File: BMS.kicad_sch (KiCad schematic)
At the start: 63 parts, among them J1 Screw_Terminal_01x02, J5 BATT_PACK -, J6 BATT_PACK -, Q22 CSD19531Q5A, Q23 CSD19531Q5A, Q24 CSD19531Q5A, T3 EE20_10_6_750811647, U1 TL431DBZ, U18 VIPer26LD, U2 PC817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

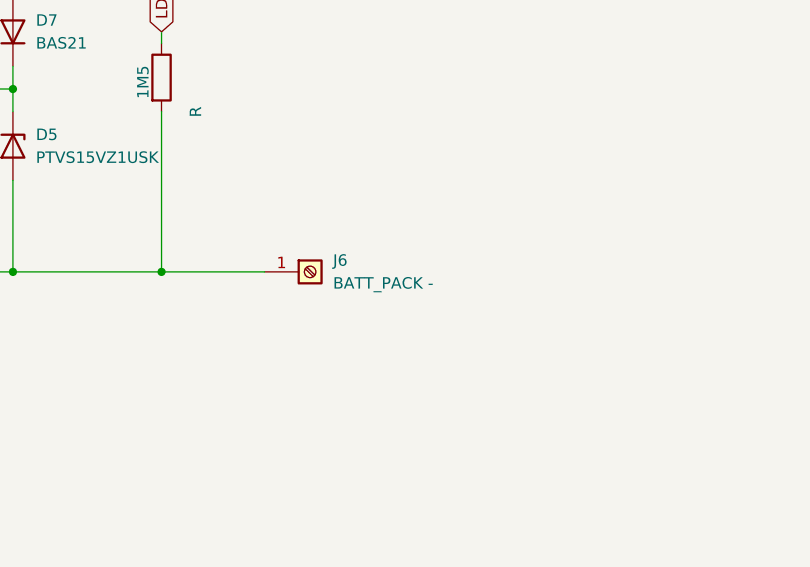
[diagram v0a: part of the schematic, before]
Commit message: Add full KiCad PCB file and backups
Replace the placeholder BMS.kicad_pcb with the complete KiCad PCB data (version 20260206) including layers, setup, footprints, pads and 3D models. Update related project files (BMS.kicad_prl, BMS.kicad_pro, BMS.kicad_sch) and their lock files. Add five new backup archives in BMS-backups (2026-06-19 and multiple 2026-06-20 timestamps).
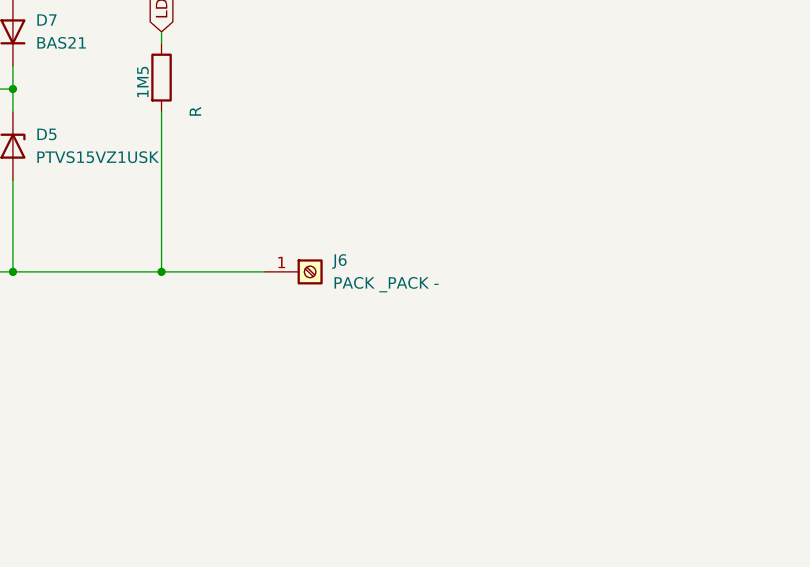
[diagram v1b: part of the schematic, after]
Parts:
- C19, C20, C24, C30, C31, C33, C34, C35, C36, C37, C38: footprint Capacitor_THT:CP_Radial_D5.0mm_P2.00mm -> Capacitor_SMD:C_0402_1005Metric
- J6: value BATT_PACK - -> PACK _PACK -
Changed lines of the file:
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@@
 			)
 		)
-		(property "Value" "BATT_PACK -"
+		(property "Value" "PACK _PACK -"
 			(at 280.67 179.0699 0)
 			(show_name no)
@@
 			)
 		)
-		(property "Footprint" "Capacitor_THT:CP_Radial_D5.0mm_P2.00mm"
+		(property "Footprint" "Capacitor_SMD:C_0402_1005Metric"
 			(at 204.47 204.1652 0)
 			(hide yes)
@@
 			)
 		)
-		(property "Footprint" "Capacitor_THT:CP_Radial_D5.0mm_P2.00mm"
+		(property "Footprint" "Capacitor_SMD:C_0402_1005Metric"
 			(at 127.9652 83.82 0)
 			(hide yes)
@@
 			)
 		)
-		(property "Footprint" "Capacitor_THT:CP_Radial_D5.0mm_P2.00mm"
+		(property "Footprint" "Capacitor_SMD:C_0402_1005Metric"
 			(at 84.1248 219.71 0)
 			(hide yes)
@@
 			)
 		)
-		(property "Footprint" "Capacitor_THT:CP_Radial_D5.0mm_P2.00mm"
+		(property "Footprint" "Capacitor_SMD:C_0402_1005Metric"
 			(at 66.3448 177.8 0)
 			(hide yes)
@@
 			)
 		)
-		(property "Footprint" "Capacitor_THT:CP_Radial_D5.0mm_P2.00mm"
+		(property "Footprint" "Capacitor_SMD:C_0402_1005Metric"
 			(at 222.25 204.1652 0)
 			(hide yes)
@@
 			)
 		)
-		(property "Footprint" "Capacitor_THT:CP_Radial_D5.0mm_P2.00mm"
+		(property "Footprint" "Capacitor_SMD:C_0402_1005Metric"
 			(at 58.42 157.7848 0)
 			(hide yes)
@@
 			)
 		)
-		(property "Footprint" "Capacitor_THT:CP_Radial_D5.0mm_P2.00mm"
+		(property "Footprint" "Capacitor_SMD:C_0402_1005Metric"
 			(at 72.6948 194.31 0)
 			(hide yes)
@@
 			)
 		)
-		(property "Footprint" "Capacitor_THT:CP_Radial_D5.0mm_P2.00mm"
+		(property "Footprint" "Capacitor_SMD:C_0402_1005Metric"
 			(at 182.88 29.5148 0)
 			(hide yes)
@@
 			)
 		)
-		(property "Footprint" "Capacitor_THT:CP_Radial_D5.0mm_P2.00mm"
+		(property "Footprint" "Capacitor_SMD:C_0402_1005Metric"
 			(at 130.5052 46.99 0)
 			(hide yes)
@@
 			)
 		)
-		(property "Footprint" "Capacitor_THT:CP_Radial_D5.0mm_P2.00mm"
+		(property "Footprint" "Capacitor_SMD:C_0402_1005Metric"
 			(at 79.0448 207.01 0)
 			(hide yes)
@@
 			)
 		)
-		(property "Footprint" "Capacitor_THT:CP_Radial_D5.0mm_P2.00mm"
+		(property "Footprint" "Capacitor_SMD:C_0402_1005Metric"
 			(at 44.7548 146.05 0)
 			(hide yes)

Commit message: Battery level indicator LM3914
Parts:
- added C3: 470uF, Capacitor_SMD:C_0805_2012Metric, symbol Device:C_Polarized
- added D10, D11, D12, D13, D14, D15, D16, D6, D8, D9: LED, symbol Device:LED
- added U3: LM3914N, Package_DIP:DIP-18_W7.62mm, symbol Driver_LED:LM3914N
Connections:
- net GND: now also U3.2 (V-)
- net V+: now reaches 2W,5.1Ohm22.2, BT18.1 (+)
- net V+: now also U3.3 (V+)
- new net: D9.1 (K), U3.17 (LED3)
- new net: C3.1, D10.2 (A), D11.2 (A), D12.2 (A), D13.2 (A), D14.2 (A), D15.2 (A), D16.2 (A), D6.2 (A), D8.2 (A), D9.2 (A)
- new net: D13.1 (K), U3.13 (LED7)
- new net: D15.1 (K), U3.11 (LED9)
- new net: D16.1 (K), U3.10 (LED10)
- new net: C3.2, U3.4 (RLO)
- new net: D12.1 (K), U3.14 (LED6)
- new net: D11.1 (K), U3.15 (LED5)
- new net: D10.1 (K), U3.16 (LED4)
- new net: D8.1 (K), U3.18 (LED2)
- new net: D6.1 (K), U3.1 (LED1)
- new net: D14.1 (K), U3.12 (LED8)

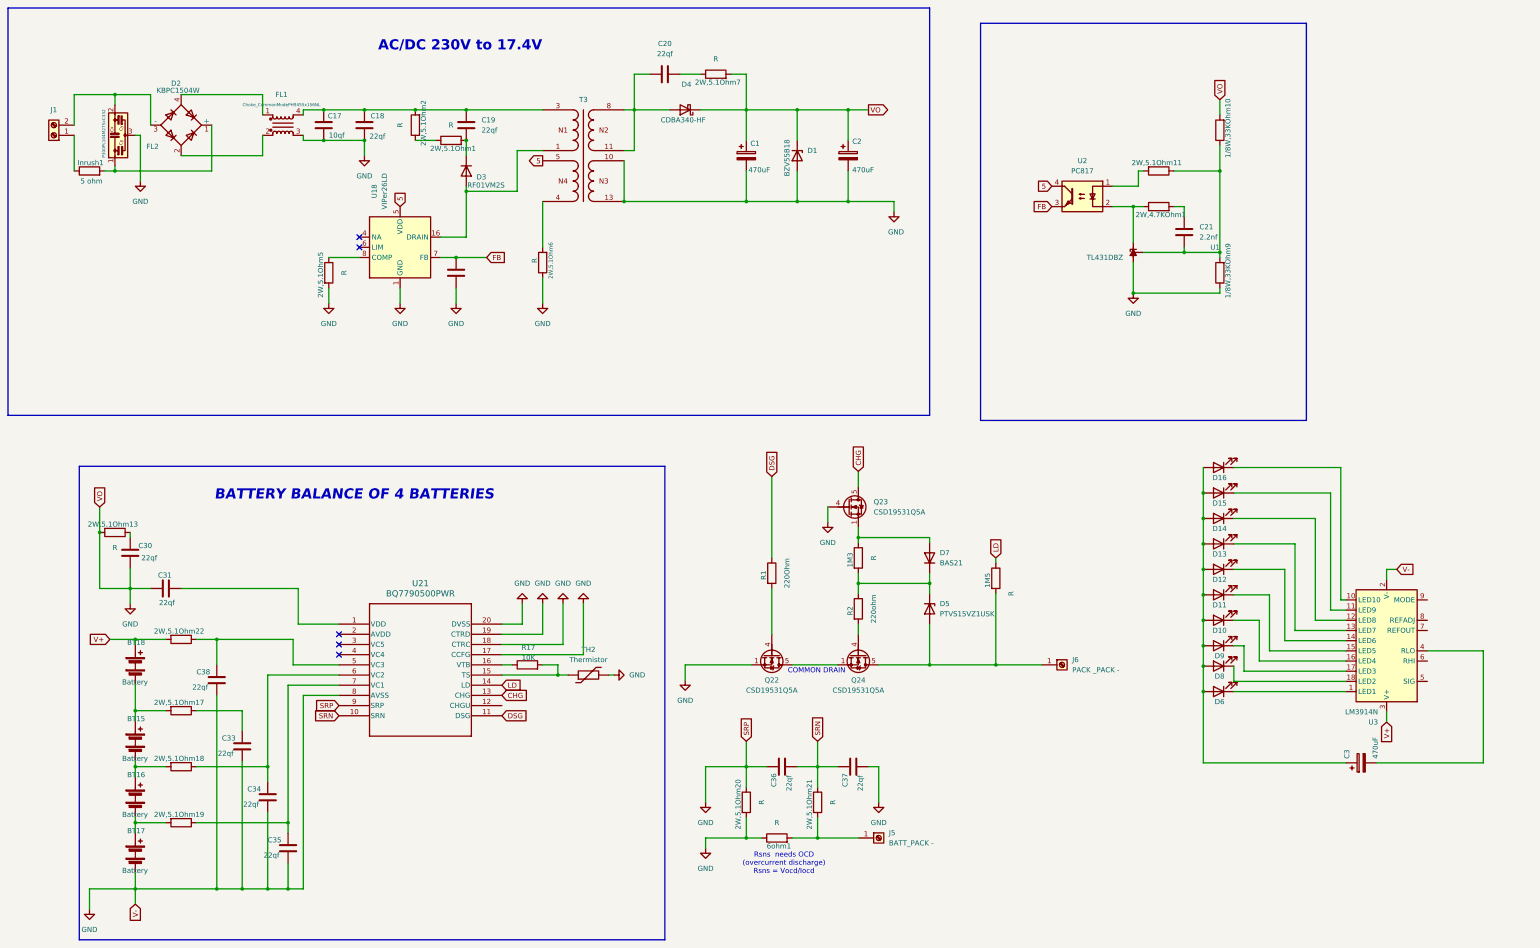
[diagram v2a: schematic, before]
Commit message: Update PCB stackup, footprints, and add backups
Add multiple BMS backup archives and project PNG; modify BMS.kicad_pcb with an explicit stackup (layers, thicknesses, dielectric), enable zone_defaults, and update many footprints and component definitions. Changes include footprint replacements and edits (resistor/pad sizes, SMD 0402→0805 adjustments, pad positions/nets, UUIDs), added/adjusted 3D model references and part rotations/offsets, and new LED/resistor SMD footprints. Also update related KiCad project files and lock files.
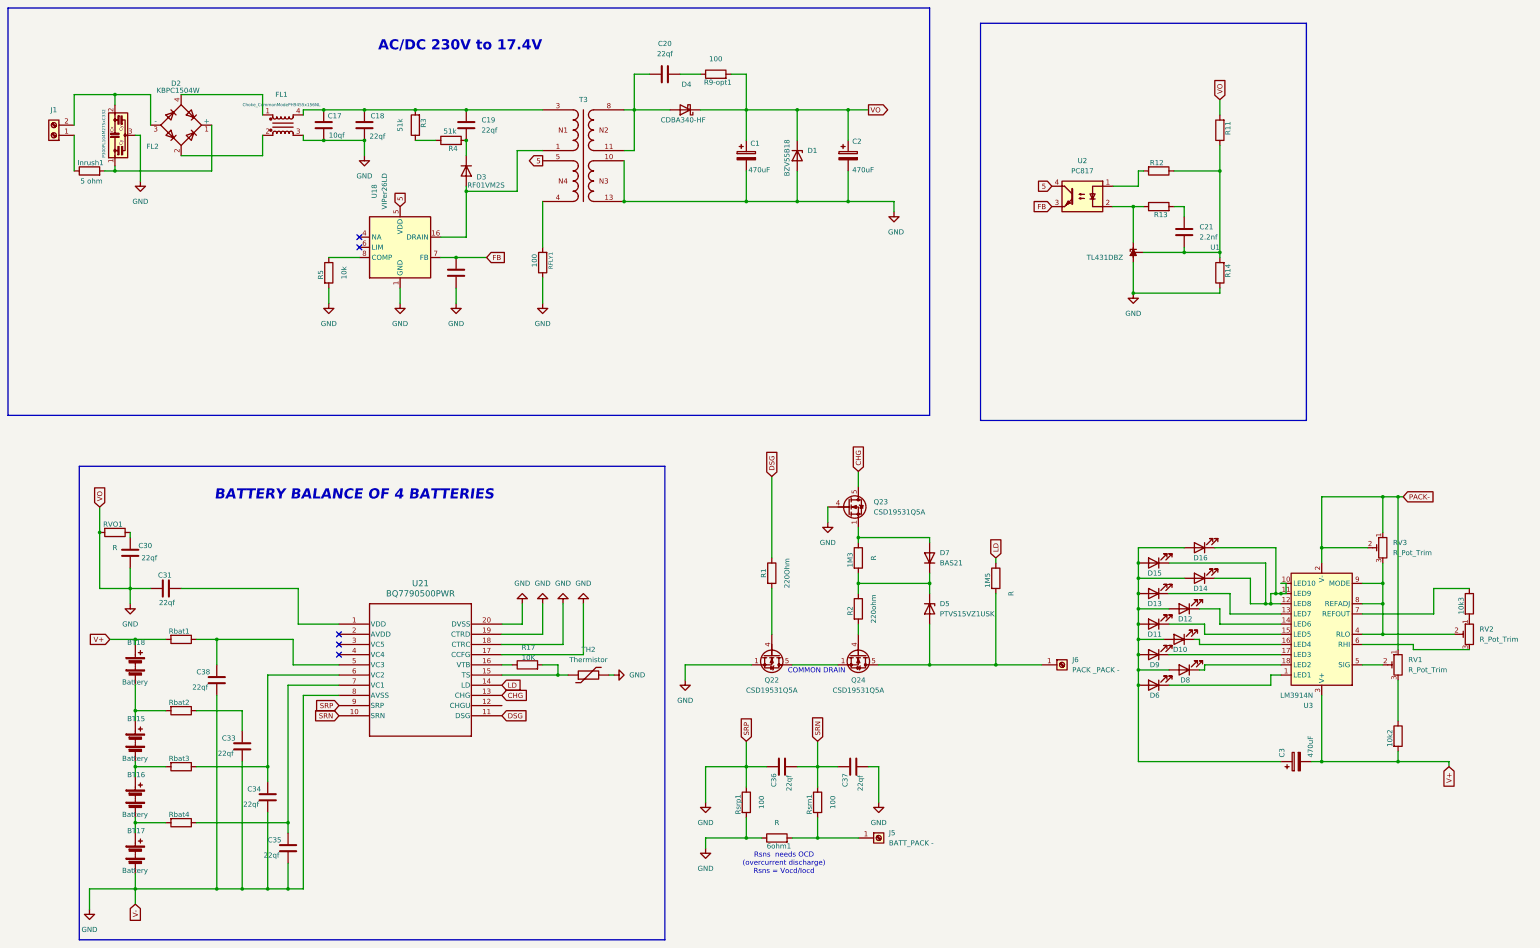
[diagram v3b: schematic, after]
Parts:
- removed 2W,5.1Ohm17, 2W,5.1Ohm18, 2W,5.1Ohm19: R, Resistor_SMD:R_0603_1608Metric, symbol Device:R
- added 10k2, 10k3: 10k, Resistor_SMD:R_0805_2012Metric, symbol Device:R
- added RV1, RV2, RV3: R_Pot_Trim, symbol Device:R_Potentiometer_Trim
- added Rbat2, Rbat3, Rbat4: 1k, Resistor_SMD:R_0805_2012Metric, symbol Device:R
- 1M3, 1M5, 6ohm1: footprint Resistor_SMD:R_0603_1608Metric -> Resistor_SMD:R_0805_2012Metric
- C20: footprint Capacitor_SMD:C_0402_1005Metric -> Capacitor_SMD:C_0805_2012Metric
- C21: footprint Capacitor_THT:CP_Radial_D5.0mm_P2.00mm -> Capacitor_SMD:C_0805_2012Metric
- D10, D11, D12, D13, D14, D15, D16, D6, D8, D9: footprint (none) -> LED_SMD:LED_0805_2012Metric
- J1: footprint TerminalBlock_MetzConnect:TerminalBlock_MetzConnect_360291_1x01_Horizontal_ScrewM3.0_Boxed -> TerminalBlock_Phoenix:TerminalBlock_Phoenix_MKDS-1,5-2_1x02_P5.00mm_Horizontal
- R1, R2: footprint Resistor_THT:R_Axial_DIN0414_L11.9mm_D4.5mm_P15.24mm_Horizontal -> Resistor_SMD:R_0805_2012Metric
- R11: renamed from 1/8W,33KOhm10; footprint Resistor_SMD:R_0603_1608Metric -> Resistor_SMD:R_0805_2012Metric
- R12: renamed from 2W,5.1Ohm11; footprint Resistor_SMD:R_0603_1608Metric -> Resistor_SMD:R_0805_2012Metric
- R13: renamed from 2W,4.7KOhm1; footprint Resistor_SMD:R_0603_1608Metric -> Resistor_SMD:R_0805_2012Metric
- R14: renamed from 1/8W,33KOhm9; footprint Resistor_SMD:R_0603_1608Metric -> Resistor_SMD:R_0805_2012Metric
- R3: renamed from 2W,5.1Ohm2; value R -> 51k; footprint Resistor_SMD:R_0603_1608Metric -> Resistor_SMD:R_0805_2012Metric
- R4: renamed from 2W,5.1Ohm1; value R -> 51k; footprint Resistor_SMD:R_0603_1608Metric -> Resistor_SMD:R_0805_2012Metric
- R5: renamed from 2W,5.1Ohm5; value R -> 10k; footprint Resistor_SMD:R_0603_1608Metric -> Resistor_SMD:R_0805_2012Metric
- R9-opt1: renamed from 2W,5.1Ohm7; value R -> 100; footprint Resistor_SMD:R_0603_1608Metric -> Resistor_SMD:R_0805_2012Metric
- RFLY1: renamed from 2W,5.1Ohm6; value R -> 100; footprint Resistor_SMD:R_0603_1608Metric -> Resistor_SMD:R_0805_2012Metric
- RVO1: renamed from 2W,5.1Ohm13; footprint Resistor_SMD:R_0603_1608Metric -> Resistor_SMD:R_0805_2012Metric
- Rbat1: renamed from 2W,5.1Ohm22; value R -> 1k; footprint Resistor_SMD:R_0603_1608Metric -> Resistor_SMD:R_0805_2012Metric
- Rsrn1: renamed from 2W,5.1Ohm21; value R -> 100; footprint Resistor_SMD:R_0603_1608Metric -> Resistor_SMD:R_0805_2012Metric
- Rsrp1: renamed from 2W,5.1Ohm20; value R -> 100; footprint Resistor_SMD:R_0603_1608Metric -> Resistor_SMD:R_0805_2012Metric
- U21: footprint PW20_TEX -> Package_SO:TSSOP-20_4.4x6.5mm_P0.65mm
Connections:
- net GND: no longer U3.2 (V-)
- net V+: now also C3.2, 10k2.2
- net at C33.2: now also Rbat2.1
- net at BT15.1 (+), BT18.2 (-): now also Rbat2.2
- net at BT16.2 (-), BT17.1 (+): now also Rbat4.2
- net at D15.1 (K), U3.11 (LED9): now also D14.1 (K), D16.1 (K), U3.10 (LED10), U3.12 (LED8)
- net at BT15.2 (-), BT16.1 (+): now also Rbat3.2
- net at C35.2, U21.7 (VC1): now also Rbat4.1
- net at U3.4 (RLO): now also U3.8 (REFADJ), U3.9 (MODE), RV2.2, RV3.3; no longer C3.2
- net at C34.2, U21.6 (VC2): now also Rbat3.1
- net at U3.5 (SIG): now also RV1.2
- net at U3.6 (RHI): now also RV2.3
- net at U3.7 (REFOUT): now also 10k3.1
- new net: 10k3.2, RV2.1
- new net: 10k2.1, RV1.3
- new net PACK-: RV1.1, RV3.1, RV3.2, U3.2 (V-)

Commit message: Update of routing
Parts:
- added R6: 100 Ohm, Resistor_SMD:R_0805_2012Metric, symbol Device:R
- C19, C24: footprint Capacitor_SMD:C_0402_1005Metric -> Capacitor_THT:CP_Radial_D5.0mm_P2.00mm
- Inrush1: footprint Resistor_THT:R_Axial_DIN0414_L11.9mm_D4.5mm_P25.40mm_Horizontal -> Resistor_THT:R_Axial_DIN0204_L3.6mm_D1.6mm_P5.08mm_Horizontal
- TH2: footprint (none) -> Resistor_SMD:R_0805_2012Metric
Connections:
- net GND: now also R6.2; no longer C36.2, Q23.4 (G), Rsrp1.1, U21.9 (SRP)
- net SRN: now also C36.2; no longer C36.1
- net V-: now reaches 1M5.2, D5.2 (A), J6.1 (Pin_1), Q24.5 (D)
- net at R9-opt1.1: now also C20.1; no longer C20.2
- net at D4.2 (A), T3.11, T3.8: now also C20.2; no longer C20.1
- net 5 renamed VDD_U18
- new net: D16.1 (K), U3.10 (LED10)
- new net: D15.1 (K), U3.11 (LED9)
- new net: D14.1 (K), U3.12 (LED8)
- new net: Q23.4 (G), R6.1
- new net SRP: C36.1, Rsrp1.1, U21.9 (SRP)
- no-connect marks 5 -> 6
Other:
- moved on the sheet: C20, C36, D16

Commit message: Updated GND via and holes
GND was missdirected at VO point and had to be fixed
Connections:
- net FB: now also U2.2; no longer U2.3
- net GND: no longer C1.1, C2.1, C31.1, D1.1 (K), D4.1 (K), R11.2, R9-opt1.2, RVO1.2
- net VDD_U18: now also U2.1; no longer U2.4
- net at R12.2: now also U2.4; no longer U2.1
- net at R13.1, U1.1 (K): now also U2.3; no longer U2.2
- new net VO: C1.1, C2.1, C31.1, D1.1 (K), D4.1 (K), R11.2, R9-opt1.2, RVO1.2
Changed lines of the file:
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@@
 	)
 	(junction
-		(at 45.72 158.75)
-		(diameter 0)
-		(color 0 0 0 0)
-	)
-	(junction
 		(at 73.66 233.68)
 		(diameter 0)
@@
 	(wire
 		(pts
-			(xy 50.8 158.75) (xy 45.72 158.75)
-		)
-		(stroke
-			(width 0)
-			(type default)
-		)
-	)
-	(wire
-		(pts
 			(xy 67.31 185.42) (xy 67.31 233.68)
 		)
@@
 	(wire
 		(pts
-			(xy 45.72 153.67) (xy 45.72 158.75)
-		)
-		(stroke
-			(width 0)
-			(type default)
-		)
-	)
-	(wire
-		(pts
 			(xy 31.75 54.61) (xy 31.75 45.72)
 		)
@@
 	(wire
 		(pts
-			(xy 45.72 158.75) (xy 38.1 158.75)
+			(xy 38.1 158.75) (xy 50.8 158.75)
 		)
 		(stroke
@@
 	(wire
 		(pts
-			(xy 45.72 158.75) (xy 45.72 162.56)
+			(xy 45.72 153.67) (xy 45.72 162.56)
 		)
 		(stroke
@@
 		(lib_id "Isolator:PC817")
 		(at 283.21 60.96 0)
-		(mirror y)
 		(unit 1)
 		(body_style 1)
@@
 		(in_pos_files yes)
 		(dnp no)
-		(fields_autoplaced yes)
 		(property "Reference" "U2"
 			(at 283.21 52.07 0)
@@
 		)
 		(property "Footprint" "Package_DIP:DIP-4_W7.62mm"
-			(at 288.29 66.04 0)
+			(at 278.13 66.04 0)
 			(hide yes)
 			(show_name no)

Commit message: Routing update
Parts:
- removed J6: PACK _PACK -, TerminalBlock_MetzConnect:TerminalBlock_MetzConnect_360271_1x01_Horizontal_ScrewM3.0_Boxed, symbol Connector:Screw_Terminal_01x01
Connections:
- net V- is gone; now on net PACK-: 1M5.2, D5.2 (A), Q24.5 (D)
- net FB: now also U2.3; no longer U2.2
- net PACK-: now also 6ohm1.2, J5.1 (Pin_1), Rsrn1.2
- net VDD_U18: now also U2.4; no longer U2.1
- net at R12.2: now also U2.1; no longer U2.4
- net at R13.1, U1.1 (K): now also U2.2; no longer U2.3
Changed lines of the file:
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@@
 	)
 	(junction
+		(at 226.06 220.98)
+		(diameter 0)
+		(color 0 0 0 0)
+	)
+	(junction
 		(at 46.99 171.45)
 		(diameter 0)
@@
 	(wire
 		(pts
+			(xy 261.62 177.8) (xy 280.67 177.8)
+		)
+		(stroke
+			(width 0)
+			(type default)
+		)
+	)
+	(wire
+		(pts
 			(xy 374.65 203.2) (xy 374.65 201.93)
 		)
@@
 	(wire
 		(pts
-			(xy 217.17 220.98) (xy 227.33 220.98)
+			(xy 217.17 220.98) (xy 226.06 220.98)
 		)
 		(stroke
@@
 	(wire
 		(pts
+			(xy 226.06 220.98) (xy 227.33 220.98)
+		)
+		(stroke
+			(width 0)
+			(type default)
+		)
+	)
+	(wire
+		(pts
 			(xy 210.82 177.8) (xy 222.25 177.8)
 		)
@@
 	(wire
 		(pts
-			(xy 261.62 177.8) (xy 273.05 177.8)
-		)
-		(stroke
-			(width 0)
-			(type default)
-		)
-	)
-	(wire
-		(pts
 			(xy 46.99 203.2) (xy 54.61 203.2)
 		)
@@
 	(wire
 		(pts
+			(xy 226.06 228.6) (xy 226.06 220.98)
+		)
+		(stroke
+			(width 0)
+			(type default)
+		)
+	)
+	(wire
+		(pts
 			(xy 212.09 203.2) (xy 217.17 203.2)
 		)
@@
 		)
 	)
+	(global_label "PACK-"
+		(shape input)
+		(at 280.67 177.8 0)
+		(fields_autoplaced yes)
+		(effects
+			(font
+				(size 1.27 1.27)
+			)
+			(justify left)
+		)
+		(property "Intersheetrefs" "${INTERSHEET_REFS}"
+			(at 290.1262 177.8 0)
+			(hide yes)
+			(show_name no)
+			(do_not_autoplace no)
+			(effects
+				(font
+					(size 1.27 1.27)
+				)
+				(justify left)
+			)
+		)
+	)
 	(global_label "FB"
 		(shape input)
@@
 		)
 	)
+	(global_label "PACK-"
+		(shape input)
+		(at 226.06 228.6 270)
+		(fields_autoplaced yes)
+		(effects
+			(font
+				(size 1.27 1.27)
+			)
+			(justify right)
+		)
+		(property "Intersheetrefs" "${INTERSHEET_REFS}"
+			(at 226.06 238.0562 90)
+			(hide yes)
+			(show_name no)
+			(do_not_autoplace no)
+			(effects
+				(font
+					(size 1.27 1.27)
+				)
+				(justify right)
+			)
+		)
+	)
 	(symbol
 		(lib_id "Device:Thermistor")
@@
 	)
 	(symbol
-		(lib_id "Connector:Screw_Terminal_01x01")
-		(at 278.13 177.8 0)
-		(unit 1)
-		(body_style 1)
-		(exclude_from_sim no)
-		(in_bom yes)
-		(on_board yes)
-		(in_pos_files yes)
-		(dnp no)
-		(fields_autoplaced yes)
-		(property "Reference" "J6"
-			(at 280.67 176.5299 0)
-			(show_name no)
-			(do_not_autoplace no)
-			(effects
-				(font
-					(size 1.27 1.27)
-				)
-				(justify left)
-			)
-		)
-		(property "Value" "PACK _PACK -"
-			(at 280.67 179.0699 0)
-			(show_name no)
-			(do_not_autoplace no)
-			(effects
-				(font
-					(size 1.27 1.27)
-				)
-				(justify left)
-			)
-		)
-		(property "Footprint" "TerminalBlock_MetzConnect:TerminalBlock_MetzConnect_360271_1x01_Horizontal_ScrewM3.0_Boxed"
-			(at 278.13 177.8 0)
-			(hide yes)
-			(show_name no)
-			(do_not_autoplace no)
-			(effects
-				(font
-					(size 1.27 1.27)
-				)
-			)
-		)
-		(property "Datasheet" ""
-			(at 278.13 177.8 0)
-			(hide yes)
-			(show_name no)
-			(do_not_autoplace no)
-			(effects
-				(font
-					(size 1.27 1.27)
-				)
-			)
-		)
-		(property "Description" "Generic screw terminal, single row, 01x01, script generated (kicad-library-utils/schlib/autogen/connector/)"
-			(at 278.13 177.8 0)
-			(hide yes)
-			(show_name no)
-			(do_not_autoplace no)
-			(effects
-				(font
-					(size 1.27 1.27)
-				)
-			)
-		)
-		(pin "1"
-		)
-		(instances
-			(project "BMS"
-				(path "/817ced98-0cef-4e0f-b532-5d01d2bf5768"
-					(reference "J6")
-					(unit 1)
-				)
-			)
-		)
-	)
-	(symbol
 		(lib_id "Diode:RF01VM2S")
 		(at 129.54 54.61 270)
@@
 		(lib_id "Isolator:PC817")
 		(at 283.21 60.96 0)
+		(mirror y)
 		(unit 1)
 		(body_style 1)
@@
 		)
 		(property "Footprint" "Package_DIP:DIP-4_W7.62mm"
-			(at 278.13 66.04 0)
+			(at 288.29 66.04 0)
 			(hide yes)
 			(show_name no)
@@
 		(lib_id "Device:R")
 		(at 227.33 151.13 0)
+		(mirror y)
 		(unit 1)
 		(body_style 1)
@@
 		(dnp no)
 		(property "Reference" "1M3"
-			(at 225.298 151.638 90)
+			(at 229.362 151.638 90)
 			(show_name no)
 			(do_not_autoplace no)
@@
 		)
 		(property "Value" "R"
-			(at 231.14 151.13 90)
+			(at 223.52 151.13 90)
 			(show_name no)
 			(do_not_autoplace no)
@@
 		)
 		(property "Footprint" "Resistor_SMD:R_0805_2012Metric"
-			(at 225.552 151.13 90)
+			(at 229.108 151.13 90)
 			(hide yes)
 			(show_name no)
